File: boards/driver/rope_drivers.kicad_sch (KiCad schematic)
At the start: 0 parts

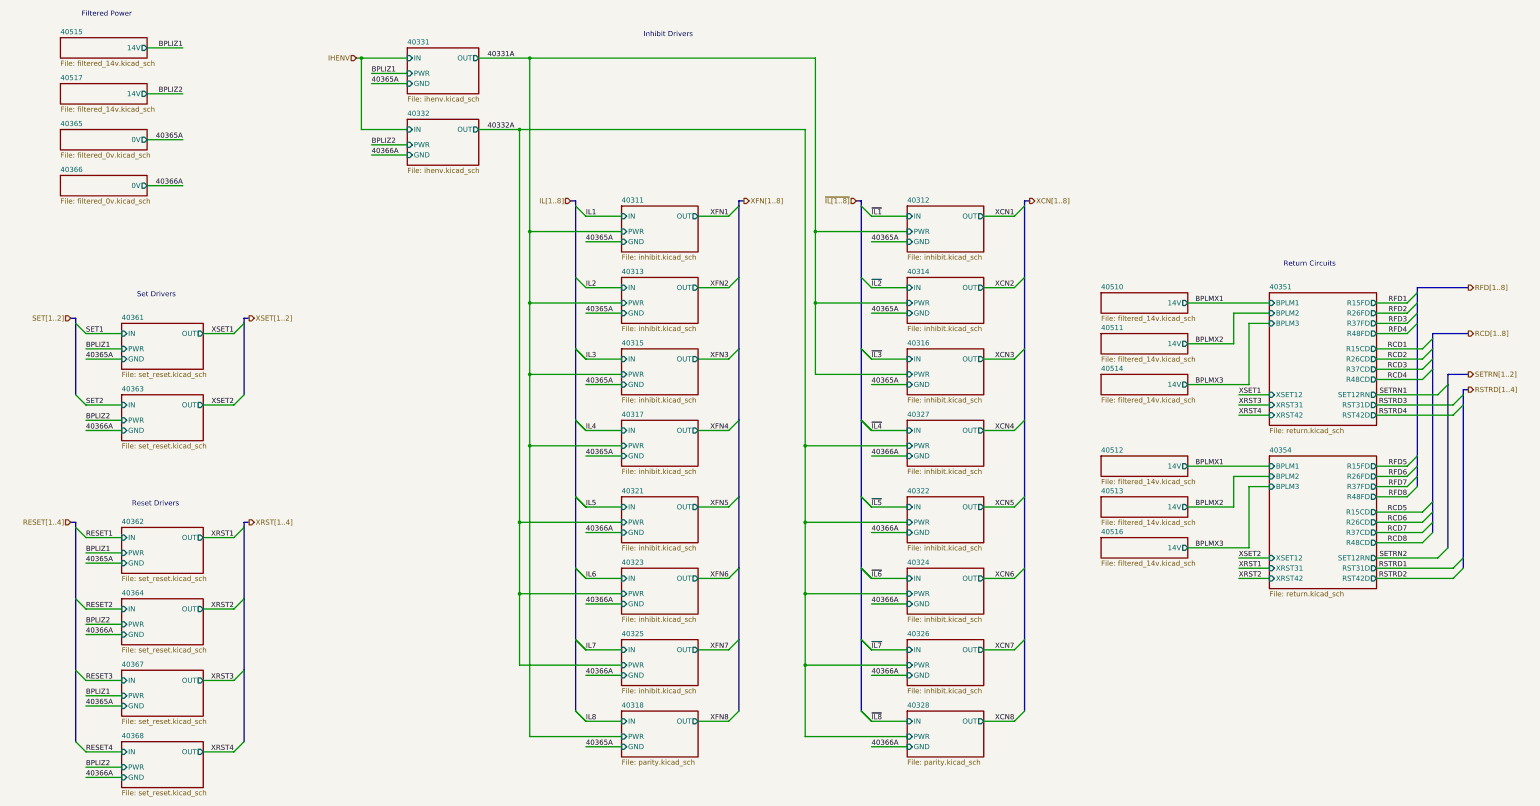
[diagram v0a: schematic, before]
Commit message: Driver: Added a 5V->3.3V LDO to replace the reversed cmod header, added jumpers for the 200R parallel returns, and renamed subcircuit ports to avoid unexpected ground connections.
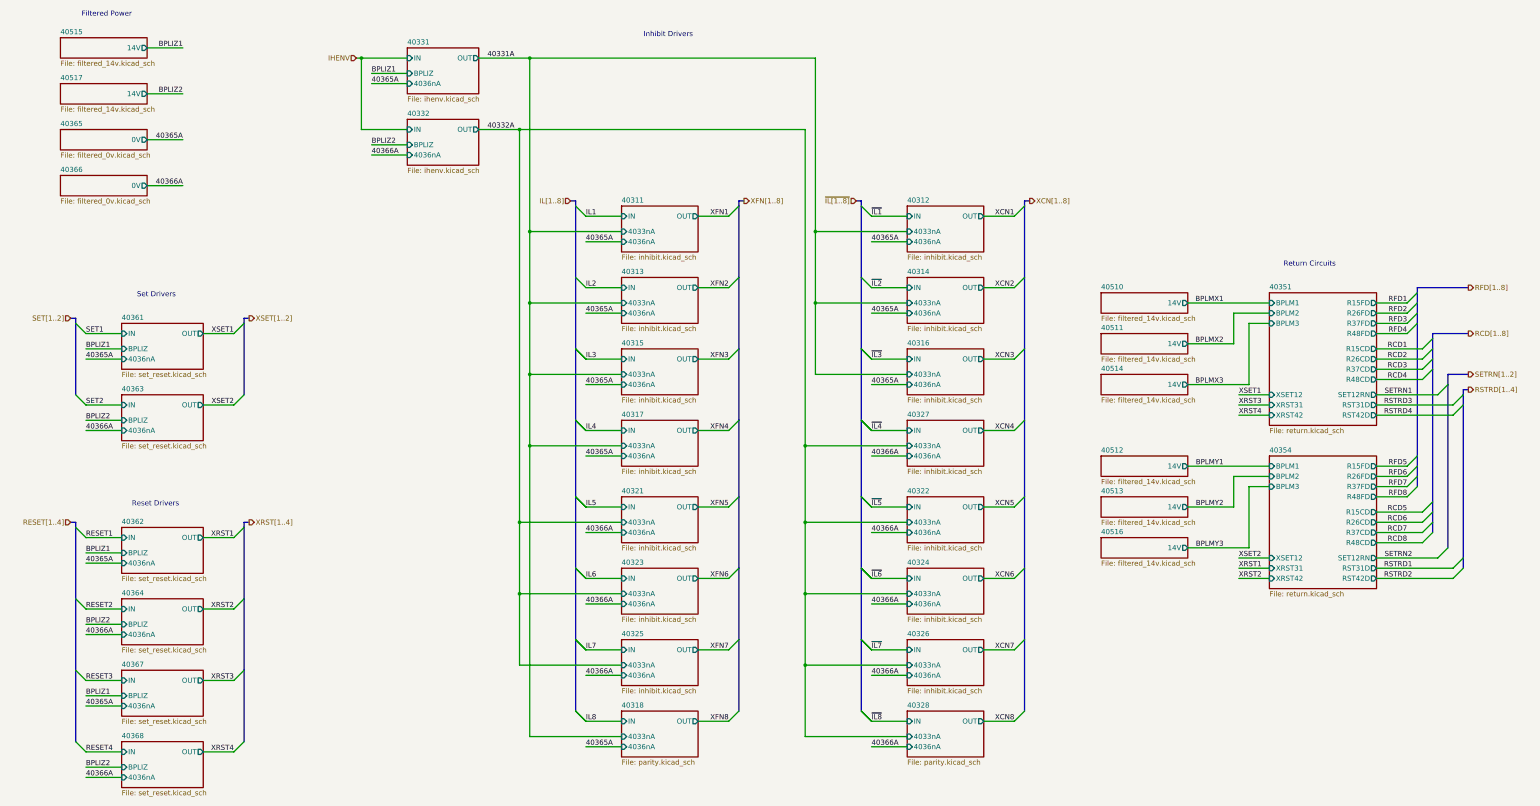
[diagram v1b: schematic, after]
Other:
- sheet 40311 ports: added 4033nA, 4036nA; removed GND, PWR
- sheet 40312 ports: added 4033nA, 4036nA; removed GND, PWR
- sheet 40313 ports: added 4033nA, 4036nA; removed GND, PWR
- sheet 40314 ports: added 4033nA, 4036nA; removed GND, PWR
- sheet 40315 ports: added 4033nA, 4036nA; removed GND, PWR
- sheet 40316 ports: added 4033nA, 4036nA; removed GND, PWR
- sheet 40317 ports: added 4033nA, 4036nA; removed GND, PWR
- sheet 40318 ports: added 4033nA, 4036nA; removed GND, PWR
- sheet 40321 ports: added 4033nA, 4036nA; removed GND, PWR
- sheet 40322 ports: added 4033nA, 4036nA; removed GND, PWR
- sheet 40323 ports: added 4033nA, 4036nA; removed GND, PWR
- sheet 40324 ports: added 4033nA, 4036nA; removed GND, PWR
- sheet 40325 ports: added 4033nA, 4036nA; removed GND, PWR
- sheet 40326 ports: added 4033nA, 4036nA; removed GND, PWR
- sheet 40327 ports: added 4033nA, 4036nA; removed GND, PWR
- sheet 40328 ports: added 4033nA, 4036nA; removed GND, PWR
- sheet 40331 ports: added 4036nA, BPLIZ; removed GND, PWR
- sheet 40332 ports: added 4036nA, BPLIZ; removed GND, PWR
- sheet 40361 ports: added 4036nA, BPLIZ; removed GND, PWR
- sheet 40362 ports: added 4036nA, BPLIZ; removed GND, PWR
- sheet 40363 ports: added 4036nA, BPLIZ; removed GND, PWR
- sheet 40364 ports: added 4036nA, BPLIZ; removed GND, PWR
- sheet 40367 ports: added 4036nA, BPLIZ; removed GND, PWR
- sheet 40368 ports: added 4036nA, BPLIZ; removed GND, PWR

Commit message: Driver: laid out most of the subcircuits
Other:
- sheet 40318: file parity.kicad_sch -> inhibit.kicad_sch
- sheet 40328: file parity.kicad_sch -> inhibit.kicad_sch

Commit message: Driver: progress on subcircuit layout and overall placement
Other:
- sheet 40331 ports: added 4033nA, IHENV; removed IN, OUT
- sheet 40332 ports: added 4033nA, IHENV; removed IN, OUT
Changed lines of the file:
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@@
       (effects (font (size 1.27 1.27)) (justify left top))
-    )
-    (pin "IN" input (at 127 33.02 180)
-      (effects (font (size 1.27 1.27)) (justify left))
-    )
-    (pin "OUT" output (at 144.78 33.02 0)
-      (effects (font (size 1.27 1.27)) (justify right))
     )
     (pin "BPLIZ" input (at 127 36.83 180)
@@
     (pin "4036nA" input (at 127 39.37 180)
       (effects (font (size 1.27 1.27)) (justify left))
+    )
+    (pin "IHENV" input (at 127 33.02 180)
+      (effects (font (size 1.27 1.27)) (justify left))
+    )
+    (pin "4033nA" output (at 144.78 33.02 0)
+      (effects (font (size 1.27 1.27)) (justify right))
     )
   )
@@
       (effects (font (size 1.27 1.27)) (justify left top))
     )
-    (pin "IN" input (at 127 50.8 180)
-      (effects (font (size 1.27 1.27)) (justify left))
-    )
-    (pin "OUT" output (at 144.78 50.8 0)
-      (effects (font (size 1.27 1.27)) (justify right))
-    )
     (pin "BPLIZ" input (at 127 54.61 180)
       (effects (font (size 1.27 1.27)) (justify left))
@@
       (effects (font (size 1.27 1.27)) (justify left))
     )
+    (pin "IHENV" input (at 127 50.8 180)
+      (effects (font (size 1.27 1.27)) (justify left))
+    )
+    (pin "4033nA" output (at 144.78 50.8 0)
+      (effects (font (size 1.27 1.27)) (justify right))
+    )
   )
